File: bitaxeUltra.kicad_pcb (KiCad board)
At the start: 4 copper layers, 56.5 x 99.8 mm, 140 parts, among them J1 PJ-037AH, J10 Conn_01x02, J2 Conn_01x02, J3 Conn_01x05, J4 Conn_01x04, J5 TC2030-IDC, J6 PJ-037AH, J7 Conn_01x02, J8 USB_C_Receptacle_USB2.0, J9 Conn_01x04, Q1 CSD17311Q5, Q2 CSD17311Q5, Q4 2N7002K, SW1 GT-TC029B-H025-L1N, SW2 GT-TC029B-H025-L1N, U1 25MHz, U10 DS4432U+, U11 RT9080-33GJ5, U12 ESP32-S3-WROOM-1, U14 BM1366_mode1, U2 TXB0104RGYR, U5 MCP1824T-1802E, U6 MCP1824T-0802E, U7 EMC2101, U8 INA260, U9 TPS40305, Y1 32.768kHz

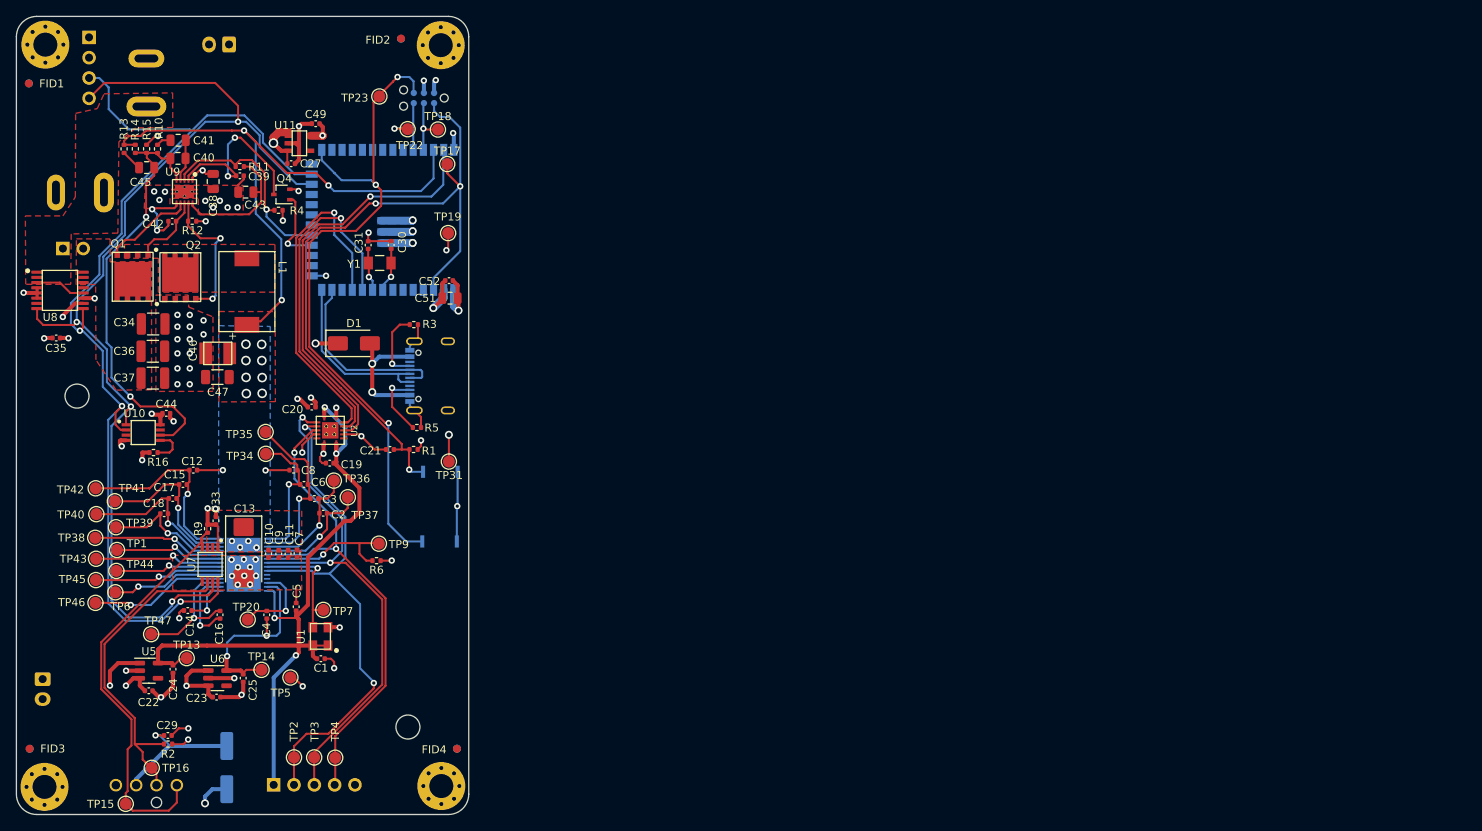
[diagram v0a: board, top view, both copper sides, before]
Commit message: added bitaxe variant for rasperry pi
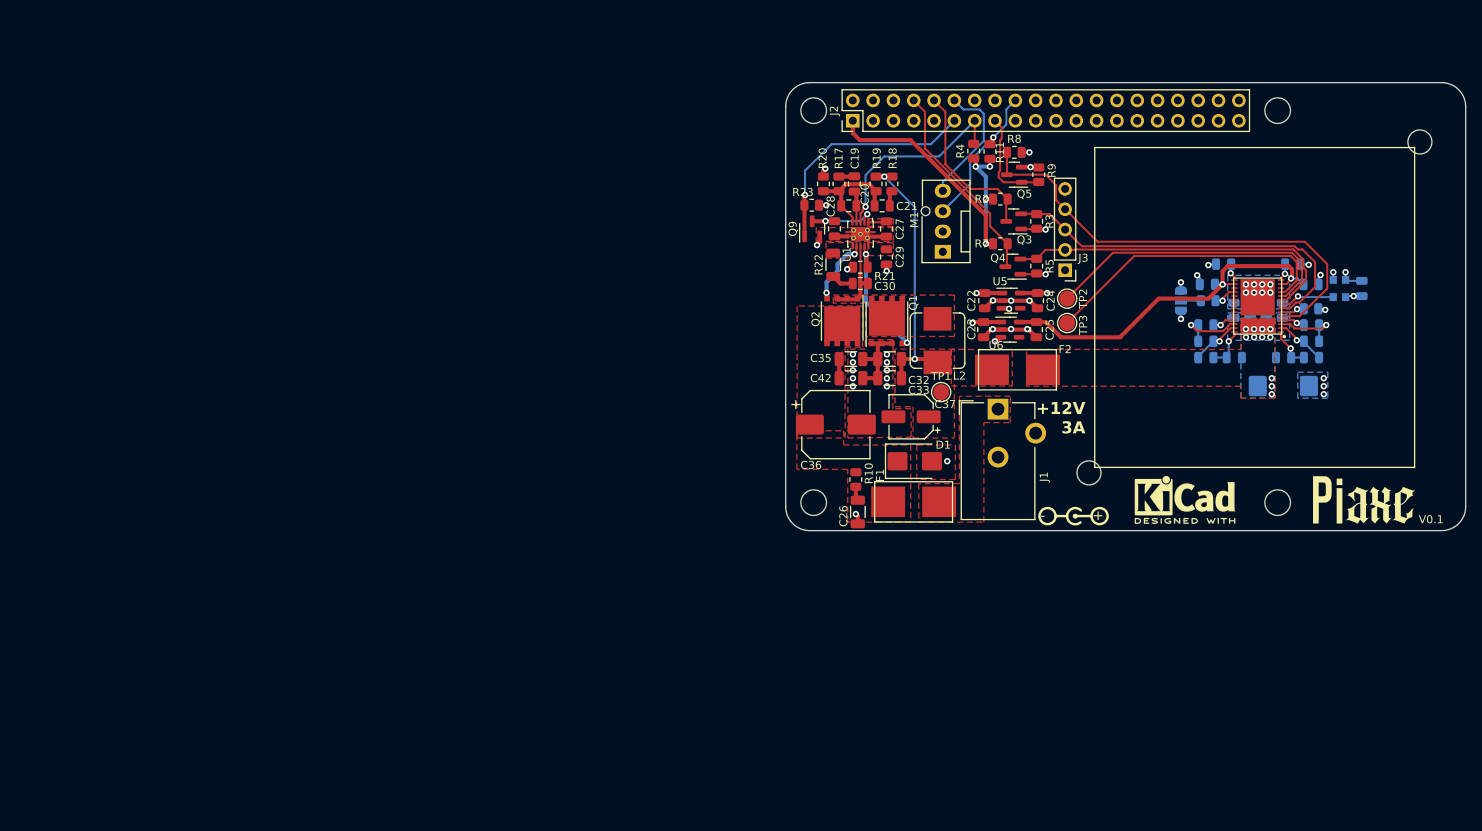
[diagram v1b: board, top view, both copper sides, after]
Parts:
- removed C31: 6.8pF, Capacitor_SMD:C_0402_1005Metric
- removed C34: 47uF, Capacitor_SMD:C_1210_3225Metric
- removed C38: 1uF, Capacitor_SMD:C_0805_2012Metric
- removed C39: 3.3nF, Capacitor_SMD:C_0402_1005Metric
- removed C40: 180pF, Capacitor_SMD:C_0805_2012Metric
- removed C41: 1.5nF, Capacitor_SMD:C_0805_2012Metric
- removed C43, C51: 10uF, Capacitor_SMD:C_0805_2012Metric
- removed C44, C49: 1uF, Capacitor_SMD:C_0402_1005Metric
- removed C45: 470pF, Capacitor_SMD:C_0805_2012Metric
- removed C46: 220uF, bitaxe:CAP_2R5TPE220MAFB
- removed C47: 100uF, Capacitor_SMD:C_1206_3216Metric
- removed C52: 0.1uF, Capacitor_SMD:C_0402_1005Metric
- removed FID1, FID2, FID3, FID4, FID5, FID6, FID7, FID8: Fiducial, Fiducial:Fiducial_1mm_Mask2mm
- removed the G*** at (95.6, 83.8)
- removed H10, H7, H8, H9: MountingHole_Pad, MountingHole:MountingHole_3mm_Pad_Via
- removed J10: Conn_01x02, bitaxe:JST_XH_B2B-XH-A_1x02_P2.50mm_Vertical
- removed J4: Conn_01x04, bitaxe:470531000
- removed J5: TC2030-IDC, bitaxe:Tag-Connect_TC2030-IDC-NL_2x03_P1.27mm_Vertical
- removed J6: PJ-037AH, bitaxe:CUI_PJ-037AH
- removed J7: Conn_01x02, Connector_PinHeader_2.54mm:PinHeader_1x02_P2.54mm_Vertical
- removed J8: USB_C_Receptacle_USB2.0, Connector_USB:USB_C_Receptacle_GCT_USB4105-xx-A_16P_TopMnt_Horizontal
- removed J9: Conn_01x04, Connector_PinHeader_2.54mm:PinHeader_1x04_P2.54mm_Vertical
- removed L1: 150nH, bitaxe:FP1005R1-R15-R
- removed R12: 4.12k, Resistor_SMD:R_0402_1005Metric
- removed R13: 1.33k, Resistor_SMD:R_0402_1005Metric
- removed R14: 4.99k, Resistor_SMD:R_0402_1005Metric
- removed R15: 3.32k, Resistor_SMD:R_0402_1005Metric
- removed R16: 80.6k, Resistor_SMD:R_0402_1005Metric
- removed SW1, SW2: GT-TC029B-H025-L1N, bitaxe:SW_CS1213AGF260_CRS
- removed TP13, TP14, TP15, TP16, TP17, TP18, TP19, TP20, TP22, TP23, TP31, TP34, TP35, TP36, TP37, TP38, TP39, TP4, TP40, TP41, TP42, TP43, TP44, TP45, TP46, TP47, TP5, TP6, TP7, TP9: TestPoint, TestPoint:TestPoint_Pad_D1.5mm
- removed U10: DS4432U+, Package_SO:TSSOP-8_3x3mm_P0.65mm
- removed U11: RT9080-33GJ5, bitaxe:RT9080-33GJ5
- removed U12: ESP32-S3-WROOM-1, bitaxe:ESP32-S3-WROOM-1
- removed U2: TXB0104RGYR, bitaxe:TXB0104
- removed U8: INA260, Package_SO:TSSOP-16_4.4x5mm_P0.65mm
- removed U9: TPS40305, bitaxe:TPS40305
- removed Y1: 32.768kHz, bitaxe:SC32S-7PF20PPM
- added C26: 2.2/50V, Capacitor_SMD:C_1206_3216Metric, F.Cu at (182.4, 109.5)
- added C32: 47µ, Capacitor_SMD:C_1206_3216Metric, F.Cu at (186.3, 90.4)
- added F1: 2.5A, myfootprints:fuseholder_littlefuse_blok, F.Cu at (189.3, 108.2)
- added F2: 20A, myfootprints:fuseholder_littlefuse_blok, F.Cu at (202.3, 91.7)
- added G***: LOGO, bitaxe:piaxelogo, F.Cu at (248.9, 128.8)
- added G***: LOGO, bitaxe:piaxelogo, F.Cu at (245.6, 108.0)
- added JP1: mode, Jumper:SolderJumper-3_P1.3mm_Open_RoundedPad1.0x1.5mm, B.Cu at (222.8, 83.1)
- added L2: 300nH, Inductor_SMD:L_Bourns_SRP7028A_7.3x6.6mm, F.Cu at (192.3, 88.1)
- added M1: Fan_4pin, Connector:FanPinHeader_1x04_P2.54mm_Vertical, F.Cu at (193.0, 77.0)
- added Q3: BSS138, Package_TO_SOT_SMD:SOT-23, F.Cu at (201.9, 73.2)
- added Q5: BSS138, Package_TO_SOT_SMD:SOT-23, F.Cu at (201.9, 67.3)
- added Q9: BSS138, Package_TO_SOT_SMD:SOT-23, F.Cu at (176.7, 74.1)
- added R17: 10k, Resistor_SMD:R_0805_2012Metric, F.Cu at (180.0, 68.5)
- added R18: 1.5k, Resistor_SMD:R_0805_2012Metric, F.Cu at (186.6, 68.5)
- added R19: 10k, Resistor_SMD:R_0805_2012Metric, F.Cu at (184.6, 68.5)
- added R20: 10k, Resistor_SMD:R_0805_2012Metric, F.Cu at (178.1, 68.5)
- added R21: 4.02k, Resistor_SMD:R_0805_2012Metric, F.Cu at (182.7, 78.9)
- added R22: 2, Resistor_SMD:R_1206_3216Metric, F.Cu at (179.3, 78.6)
- added R23: 10k, Resistor_SMD:R_0805_2012Metric, F.Cu at (176.6, 71.1)
- added R7: 10k, Resistor_SMD:R_0805_2012Metric, F.Cu at (200.2, 75.9)
- added R8: 10k, Resistor_SMD:R_0805_2012Metric, F.Cu at (201.9, 64.5)
- added REF**: MountingHole_3.2mm_M3, Mounting_Holes:MountingHole_3.2mm_M3, F.Cu at (176.8, 108.3)
- added REF**: MountingHole_3.2mm_M3, Mounting_Holes:MountingHole_3.2mm_M3, F.Cu at (234.8, 108.3)
- added REF**: MountingHole_3.2mm_M3, Mounting_Holes:MountingHole_3.2mm_M3, F.Cu at (176.8, 59.3)
- added REF**: MountingHole_3.2mm_M3, Mounting_Holes:MountingHole_3.2mm_M3, F.Cu at (234.8, 59.3)
- added REF**: KiCad-Logo2_5mm_SilkScreen, Symbol:KiCad-Logo2_5mm_SilkScreen, F.Cu at (223.3, 108.0)
- C1, C7, C9: value 0.1uF -> 100n; footprint Capacitor_SMD:C_0402_1005Metric -> Capacitor_SMD:C_0805_2012Metric; moved to B.Cu
- C10, C11, C12, C14, C15, C16, C17, C18, C2, C3, C4, C5, C6, C8: value 1uF -> 1µ; footprint Capacitor_SMD:C_0402_1005Metric -> Capacitor_SMD:C_0805_2012Metric; moved to B.Cu
- C13: value 330uF -> 330µ; moved to B.Cu
- C19: value 0.1uF -> 680p; footprint Capacitor_SMD:C_0402_1005Metric -> Capacitor_SMD:C_0805_2012Metric
- C20: value 0.1uF -> 100p; footprint Capacitor_SMD:C_0402_1005Metric -> Capacitor_SMD:C_0805_2012Metric
- C21: value 1uF -> 680p; footprint Capacitor_SMD:C_0402_1005Metric -> Capacitor_SMD:C_0805_2012Metric
- C22, C23: value 0.1uF -> 100n; footprint Capacitor_SMD:C_0402_1005Metric -> Capacitor_SMD:C_0805_2012Metric
- C24, C25, C27: value 1uF -> 1µ; footprint Capacitor_SMD:C_0402_1005Metric -> Capacitor_SMD:C_0805_2012Metric
- C28: value 220uF -> 3.3n; footprint Capacitor_SMD:CP_Elec_6.3x7.7 -> Capacitor_SMD:C_0805_2012Metric; moved to F.Cu
- C29: value 0.1uF -> 1µ; footprint Capacitor_SMD:C_0402_1005Metric -> Capacitor_SMD:C_0805_2012Metric
- C30: value 6.8pF -> 100n; footprint Capacitor_SMD:C_0402_1005Metric -> Capacitor_SMD:C_0805_2012Metric
- C33: value 0.1uF -> 47µ; footprint Capacitor_SMD:C_0402_1005Metric -> Capacitor_SMD:C_1206_3216Metric
- C35: value 1uF -> 10µ; footprint Capacitor_SMD:C_0402_1005Metric -> Capacitor_SMD:C_1206_3216Metric
- C36: value 47uF -> 330µ; footprint Capacitor_SMD:C_1210_3225Metric -> Capacitor_SMD:CP_Elec_8x10
- C37: value 47uF -> 220µ; footprint Capacitor_SMD:C_1210_3225Metric -> Capacitor_SMD:CP_Elec_5x5.8
- C42: value 0.1uF -> 10µ; footprint Capacitor_SMD:C_0402_1005Metric -> Capacitor_SMD:C_1206_3216Metric
- D1: value SS310 -> SMBJ12A; footprint Diode_SMD:D_SMA -> Diode_SMD:D_SMB
- J1: value PJ-037AH -> Barrel_Jack_Switch; footprint bitaxe:CUI_PJ-037AH -> Connector_BarrelJack:BarrelJack_CUI_PJ-102AH_Horizontal; moved to F.Cu
- J2: value Conn_01x02 -> Conn_02x20_Odd_Even; footprint bitaxe:JST_XH_B2B-XH-A_1x02_P2.50mm_Vertical -> Connector_PinHeader_2.54mm:PinHeader_2x20_P2.54mm_Vertical; moved to F.Cu
- J3, U14, U3: moved to F.Cu
- Q1, Q2: value CSD17311Q5 -> CSD16321Q5; footprint bitaxe:CSD17311Q5 -> Package_SON:VSONP-8-1EP_5x6_P1.27mm
- Q4: value 2N7002K -> BSS138; footprint Package_TO_SOT_SMD:SOT-323_SC-70 -> Package_TO_SOT_SMD:SOT-23
- R1, R6: footprint Resistor_SMD:R_0402_1005Metric -> Resistor_SMD:R_0805_2012Metric; moved to B.Cu
- R10: value 3.83k -> 2k; footprint Resistor_SMD:R_0402_1005Metric -> Resistor_SMD:R_0805_2012Metric
- R11: value 100k -> 2k2; footprint Resistor_SMD:R_0402_1005Metric -> Resistor_SMD:R_0805_2012Metric
- R2: value 5.6k -> 10k; footprint Resistor_SMD:R_0402_1005Metric -> Resistor_SMD:R_0805_2012Metric
- R3, R5: value 5.1k -> 10k; footprint Resistor_SMD:R_0402_1005Metric -> Resistor_SMD:R_0805_2012Metric
- R4: footprint Resistor_SMD:R_0402_1005Metric -> Resistor_SMD:R_0805_2012Metric
- R9: value 10k -> 100k; footprint Resistor_SMD:R_0402_1005Metric -> Resistor_SMD:R_0805_2012Metric
- TP1: value TestPoint -> +1V5; footprint TestPoint:TestPoint_Pad_D1.5mm -> TestPoint:TestPoint_Pad_D2.0mm
- TP2: value TestPoint -> TEMP_P; footprint TestPoint:TestPoint_Pad_D1.5mm -> TestPoint:TestPoint_Pad_D2.0mm
- TP3: value TestPoint -> TEMP_n; footprint TestPoint:TestPoint_Pad_D1.5mm -> TestPoint:TestPoint_Pad_D2.0mm
- U1: value 25MHz -> TPS40304DRC; footprint bitaxe:O 25,0-JO32-B-1V3-1-T1-LF -> Package_SON:VSON-10-1EP_3x3mm_P0.5mm_EP1.65x2.4mm_ThermalVias
- U7: value EMC2101 -> 25MHz; footprint Package_SO:TSSOP-8_3x3mm_P0.65mm -> Oscillator:Oscillator_SMD_EuroQuartz_XO32-4Pin_3.2x2.5mm; moved to B.Cu
- moved H5 146.2 mm to (252.6, 63.3), turned to 90 degrees
- moved U7 145.3 mm to (242.6, 81.5), turned to 180 degrees
- moved C1 138.1 mm to (245.4, 81.5), turned to -90 degrees
- moved C4 136.9 mm to (239.0, 81.0), turned to 0 degrees
- moved C14 136.5 mm to (228.1, 78.5)
- moved U3 135.7 mm to (209.6, 110.0), turned to 0 degrees
- moved C18 132.3 mm to (225.9, 86.1), turned to 0 degrees
- moved C5 131.7 mm to (236.7, 78.5), turned to 0 degrees
- moved C13 131.6 mm to (235.6, 93.7), turned to 0 degrees
- moved C12 130.9 mm to (229.4, 90.2)
- moved U14 130.8 mm to (232.3, 83.7)
- moved C17 130.6 mm to (225.9, 88.1)
- moved C10 130.3 mm to (235.5, 84.3), turned to 90 degrees
- moved C16 130.1 mm to (226.1, 81.0), turned to 180 degrees
- moved C15 128.8 mm to (225.9, 90.2)
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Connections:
- net /BM1366/VDD1_0 renamed Net-(U14-VDD1_0)
- net /BM1366/VDD1_1 renamed Net-(U14-VDD1_1)
- net /BM1366/VDD2_0 renamed Net-(U14-VDD2_0)
- net /BM1366/VDD2_1 renamed Net-(U14-VDD2_1)
- net /BM1366/VDD3_0 renamed Net-(U14-VDD3_0)
- net /BM1366/VDD3_1 renamed Net-(U14-VDD3_1)
- net /BM1366/VDD4_0 renamed Net-(U14-VDD4_0)
- net /BM1366/VDD4_1 renamed Net-(U14-VDD4_1)
- net /VDD renamed +1V5
- C1 pad 1: GND -> +1V8
- C1 pad 2: /BM1366/1V8 -> GND
- C14 pad 1: Net-(U14-VDDIO_18_1) -> +1V8
- C16 pad 1: /BM1366/MODE_1 -> +0V8
- C16 pad 2: Net-(U14-VDDIO_08_1) -> GND
- C19 pad 1: /BM1366/1V8 -> Net-(U1-COMP)
- C19 pad 2: GND -> Net-(C19-Pad2)
- C20 pad 1: /3V3 -> Net-(U1-COMP)
- C20 pad 2: GND -> Net-(U1-FB)
- C21 pad 1: /ESP32/EN -> Net-(C21-Pad1)
- C21 pad 2: GND -> Net-(U1-FB)
- C22 pad 1: /5V -> +5V
- C23 pad 1: /5V -> +5V
- C24 pad 1: /BM1366/1V8 -> +1V8
- C25 pad 1: /BM1366/0V8 -> +0V8
- C27 pad 1: /5V -> Net-(U1-VDD)
- C28 pad 1: /5V -> Net-(Q9-D)
- C29 pad 1: /5V -> Net-(U1-BP)
- C30 pad 1: /ESP32/XIN32 -> Net-(C30-Pad1)
- C30 pad 2: GND -> Net-(Q1-D)
- C33 pad 1: /3V3 -> Net-(C32-Pad1)
- C35 pad 1: /3V3 -> +12V
- C36 pad 1: /5V -> +12V
- C37 pad 1: /5V -> Net-(C32-Pad1)
- C4 pad 1: /BM1366/MODE_OUT -> +0V8
- C4 pad 2: /BM1366/0V8 -> GND
- C42 pad 1: Net-(U9-BOOT) -> +12V
- C42 pad 2: /Power/SW -> GND
- C5 pad 1: /BM1366/1V8 -> +1V8
- D1 pad 1: /5V -> +12V
- D1 pad 2: Net-(D1-Pad2) -> GND
- J1 pad 1: /Power/VIN -> Net-(F1-Pad2)
- J2 pad 1: GND -> +3V3
- J2 pad 2: /5V -> +5V
- J3 pad 1: /BM1366/1V8 -> +1V8
- Q1 pad 1: /Power/SW -> GND
- Q1 pad 2: /Power/SW -> Net-(Q1-G)
- Q1 pad 3: /Power/SW -> Net-(Q1-D)
- Q2 pad 1: GND -> Net-(Q1-D)
- Q2 pad 2: GND -> Net-(Q2-G)
- Q2 pad 3: GND -> +12V
- Q4 pad 1: /ESP32/PWR_EN -> +1V8
- Q4 pad 2: GND -> /BM1366/CI
- Q4 pad 3: Net-(Q4-D) -> /Pi/TXD
- R1 pad 1: /3V3 -> Net-(U14-MODE_0)
- R1 pad 2: /ESP32/EN -> Net-(JP1-C)
- R10 pad 1: Net-(C41-Pad2) -> +12V
- R10 pad 2: /Power/OUT0 -> Net-(C26-Pad1)
- R11 pad 1: /Power/PGOOD -> +3V3
- R11 pad 2: Net-(U9-BP) -> /Pi/TACHO
- R2 pad 1: /Fan/FAN_TACH -> /Pi/RXD
- R2 pad 2: /3V3 -> +3V3
- R3 pad 1: GND -> /BM1366/RO
- R3 pad 2: Net-(J8-CC1) -> +1V8
- R4 pad 1: /3V3 -> +3V3
- R4 pad 2: /Power/PGOOD -> /Pi/PGOOD
- R5 pad 1: GND -> /BM1366/CI
- R5 pad 2: Net-(J8-CC2) -> +1V8
- R9 pad 1: /Fan/FAN_PWM -> GND
- R9 pad 2: /3V3 -> /Pi/NRST
- TP1 pad 1: /BM1366/BO -> Net-(C32-Pad1)
- TP2 pad 1: /BM1366/CI -> /BM1366/TEMP_P
- TP3 pad 1: /BM1366/RO -> /BM1366/TEMP_N
- U1 pad 1: /BM1366/1V8 -> Net-(U1-VDD)
- U1 pad 2: GND -> Net-(Q9-D)
- U1 pad 3: /BM1366/CLKI -> /Pi/PGOOD
- U1 pad 4: /BM1366/1V8 -> Net-(U1-COMP)
- U14 pad 12: /BM1366/MODE_OUT -> unconnected-(U14-MODEO-Pad12)
- U14 pad 13: /BM1366/0V8 -> +0V8
- U14 pad 14: /BM1366/1V8 -> +1V8
- U14 pad 15: Net-(U14-VDDIO_18_1) -> +1V8
- U14 pad 16: Net-(U14-VDDIO_08_1) -> +0V8
- U14 pad 17: /BM1366/MODE_1 -> Net-(U14-MODE_0)
- U14 pad 18: /BM1366/MODE_0 -> Net-(U14-MODE_0)
- U14 pad 19: /BM1366/NC -> unconnected-(U14-NC-Pad19)
- U14 pad 20: /BM1366/CO -> unconnected-(U14-CO-Pad20)
- U14 pad 21: /BM1366/CLKO -> unconnected-(U14-CLKO-Pad21)
- U14 pad 22: /BM1366/RI -> unconnected-(U14-RI-Pad22)
- U14 pad 23: /BM1366/BO -> unconnected-(U14-BO-Pad23)
- U14 pad 24: /BM1366/NRSTO -> unconnected-(U14-NRSTO-Pad24)
- U5 pad 1: /5V -> +5V
- U5 pad 3: /5V -> +5V
- U5 pad 5: /BM1366/1V8 -> +1V8
- U6 pad 1: /5V -> +5V
- U6 pad 3: /5V -> +5V
- U6 pad 5: /BM1366/0V8 -> +0V8
- U7 pad 1: /3V3 -> +1V8
- U7 pad 2: unconnected-(U7-DP-Pad2) -> GND
- U7 pad 3: unconnected-(U7-DN-Pad3) -> /BM1366/CLKI
- U7 pad 4: /Fan/FAN_PWM -> +1V8
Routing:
- net /5V: track 224.6 -> 0.00 mm, vias 7 -> 0
- net /SDA: track 136.1 -> 0.00 mm, vias 4 -> 0
- net /SCL: track 130.3 -> 0.00 mm, vias 3 -> 0
- net /BM1366/1V8: track 94.1 -> 0.00 mm, vias 4 -> 0
- net /ESP32/EN: track 89.7 -> 0.00 mm, vias 3 -> 0
- net /ESP32/IO0: track 86.3 -> 0.00 mm, vias 3 -> 0
- net +1V5: track 83.2 -> 0.00 mm, vias 17 -> 11
- net /3V3: track 66.3 -> 0.00 mm, vias 14 -> 0
- net +5V: track 0.00 -> 57.8 mm, vias 0 -> 4
- net /Power/OUT0: track 54.6 -> 0.00 mm, vias 2 -> 0
- net /RST: track 52.7 -> 0.00 mm, vias 1 -> 0
- net /Fan/FAN_PWM: track 51.9 -> 0.00 mm
- net +0V8: track 0.00 -> 46.8 mm, vias 0 -> 2
- net /TX: track 43.7 -> 0.00 mm, vias 1 -> 0
- net /RX: track 43.3 -> 0.00 mm, vias 1 -> 0
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- added copper zone on F.Cu, net +12V
- added copper zone on In2.Cu, net +1V8
- added copper zone on B.Cu, net GND
- added copper zone on F.Cu, net Net-(C32-Pad1)
- added copper zone on F.Cu, net Net-(F1-Pad2)
- added copper zone on F.Cu, net Net-(Q1-D)
- added copper zone on F.Cu, net Net-(U1-BOOT)
- added copper zone on F.Cu, net Net-(U1-BP)
- added copper zone on F.Cu, net Net-(U1-VDD)
- removed copper zone on In2.Cu, net /3V3
- removed copper zone on F.Cu, net /5V
- removed copper zone on F.Cu, net /Power/SW
- removed copper zone on F.Cu, net /Power/VIN
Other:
- board size 56.5 x 99.8 mm -> 85 x 56 mm
- board text added: "+12V 3A"
- board text added: "V0.1"
- board text removed: "/ 21M"
- board text removed: "1V8"
- board text removed: "202"
- board text removed: "5V"
- board text removed: "GND"
- board text removed: "PWM"
- board text removed: "RST"
- board text removed: "RXI"
- board text removed: "TAC"
- board text removed: "TXO"
- board text removed: "∞"
